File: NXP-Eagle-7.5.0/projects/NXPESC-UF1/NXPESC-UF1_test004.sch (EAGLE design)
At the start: 63 parts, among them J2 FLH1-03SZ-S3A-T, U1 MKV31F512VLL12-M, U10 PSMN1R4-30YLD, U11 PSMN1R4-30YLD, U12 PSMN1R4-30YLD, U13 PSMN1R4-30YLD, U2 MKV31F512VLH12-M, U8 PSMN1R4-30YLD, U9 PSMN1R4-30YLD

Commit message: connected additional signals to gate driver
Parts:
- removed U1: MKV31F512VLL12-M, MKV31F512VLL12:MKV31F512VLL12-M
- added D1, D2, D3: (no value), etc-diode_002a:DIODE-SOD323-R
- added R29, R30, R31: RESC0603-100R, etc_rcl:RESC0603-100R
- added U15: TJA1042TK/3, TJA1042T:TJA1042TK/3
- added U17: DF13-4P-1.25H, pixhawk2:DF13-4P-1.25H
- C1: value (none) -> Find a 50V
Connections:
- net N$7 renamed PWM_BT
- net N$8 renamed PWM_BB
- new net +5V: U15.VCC
- new net CAN0_RX: U15.RXD, U2.PTA13/LLWU_P4
- new net CAN0_TX: U15.TXD, U2.PTA12
- new net N$15: D3.C, U$1.VB1
- new net N$16: D2.C, U$1.VB2
- new net N$18: D1.C, U$1.VB3
- new net N$22: U15.CANH, U17-2.S
- new net N$23: U15.CANL, U17-3.S
- new net N$7: D3.A, R31.2
- new net N$8: R29.1, R30.1, R31.1
- new net PWM_AB: U$1.LIN1, U2.PTC2
- new net PWM_AT: U$1.HIN1, U2.PTC1/LLWU_P6
- new net PWM_CB: U$1.LIN3, U2.PTD5
- new net PWM_CT: U$1.HIN3, U2.PTD4/LLWU_P14
- new net STB: U15.STB, U2.PTA5
- net +3V3: now also U15.VIO, U2.VDD_2, U2.VDD_3; no longer U1.VDD, U1.VDD_2, U1.VDD_4, U1.VDD_5, U1.VDD_6, U2.PTE24, U2.VSS_3
- net GND: now also U15.GND, U17-4.S, U2.VSS_2, U2.VSS_3; no longer U1.VSS, U1.VSS_2, U1.VSS_4, U1.VSS_5, U1.VSS_6, U2.PTA18, U2.PTE25
- net N$5: now also D1.A, R29.2; no longer U$1.HIN1, U1.PTC1/LLWU_P6, U2.PTC1/LLWU_P6
- net N$6: now also D2.A, R30.2; no longer U$1.LIN1, U1.PTC2, U2.PTC2
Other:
- note added: "Need to define exact pinout"
- note added: "Verify against KV11 board This GPIO picked at random"
- note added: "change to 10 ohm, check power"
- moved on the sheet: C1, U2

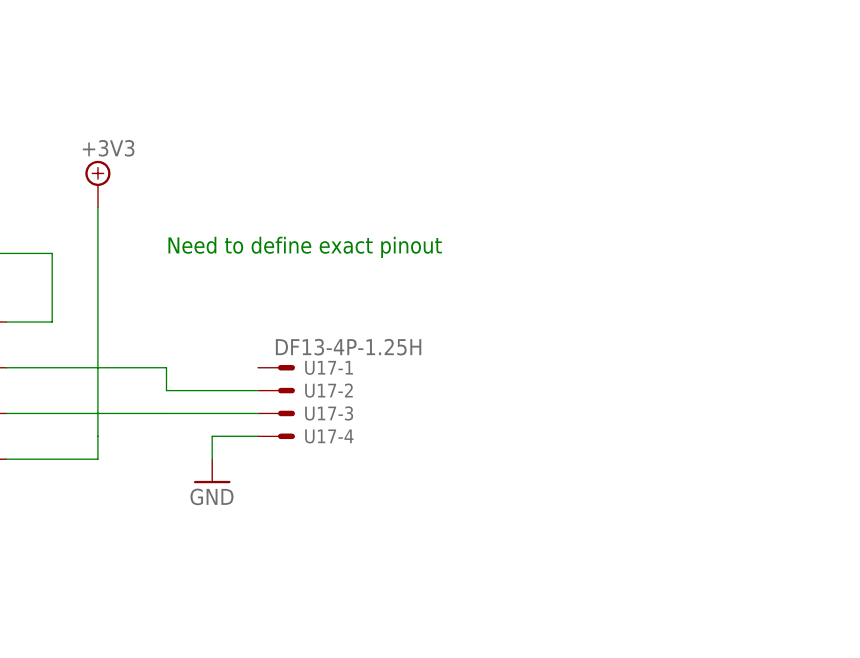
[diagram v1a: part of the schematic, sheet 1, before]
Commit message: moved from rev 003 to 004, merged in Gallowaa CAN conenctor additions.
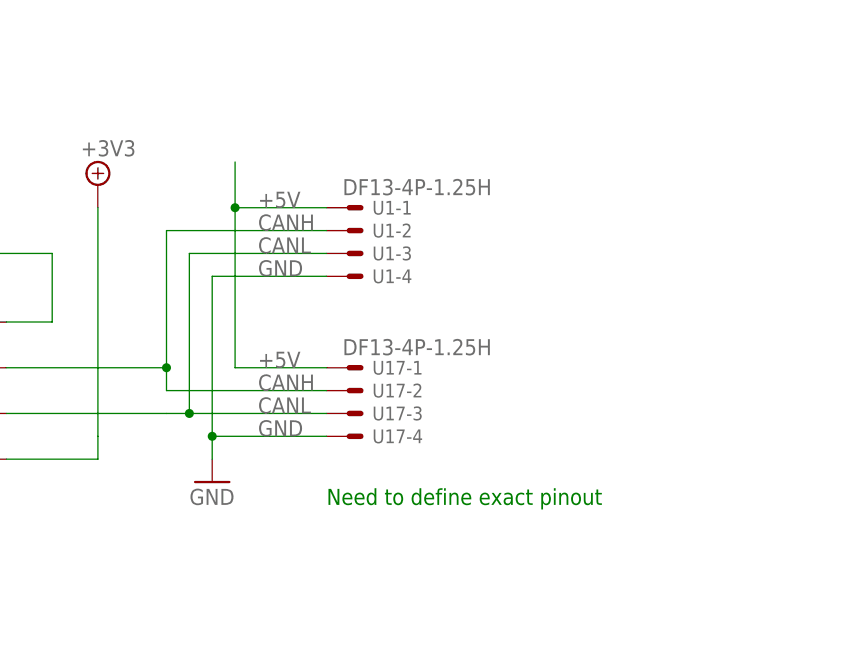
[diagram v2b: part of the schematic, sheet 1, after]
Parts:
- added U1: DF13-4P-1.25H, pixhawk2:DF13-4P-1.25H
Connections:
- removed net N$22: U15.CANH, U17-2.S
- removed net N$23: U15.CANL, U17-3.S
- new net CANH: U1-2.S, U15.CANH, U17-2.S
- new net CANL: U1-3.S, U15.CANL, U17-3.S
- net +5V: now also U1-1.S, U17-1.S
- net GND: now also U1-4.S
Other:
- moved on the sheet: U17-1, U17-2, U17-3, U17-4

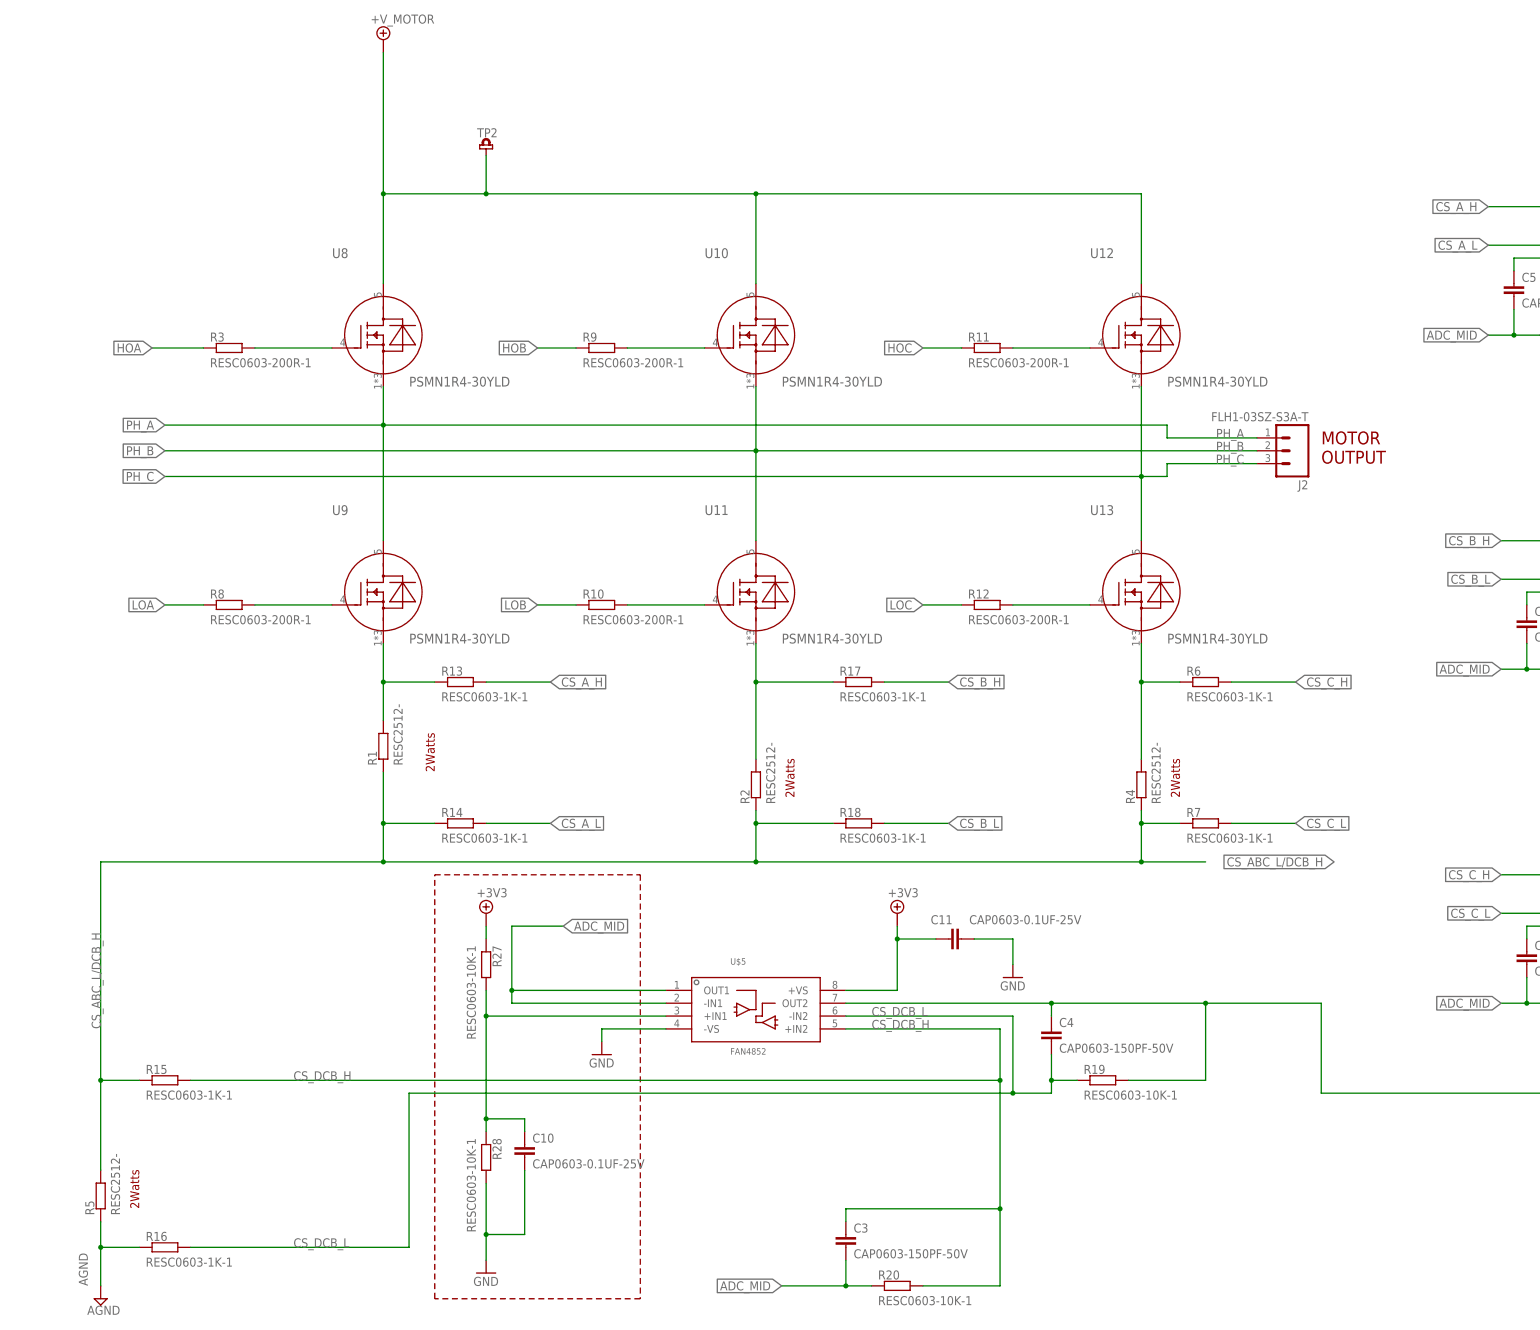
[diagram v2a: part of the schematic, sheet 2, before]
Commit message: more test routing. layout is tight but looks possible. Need to switch back to schematic to add missing parts (regulators, connectors, capacitors.)
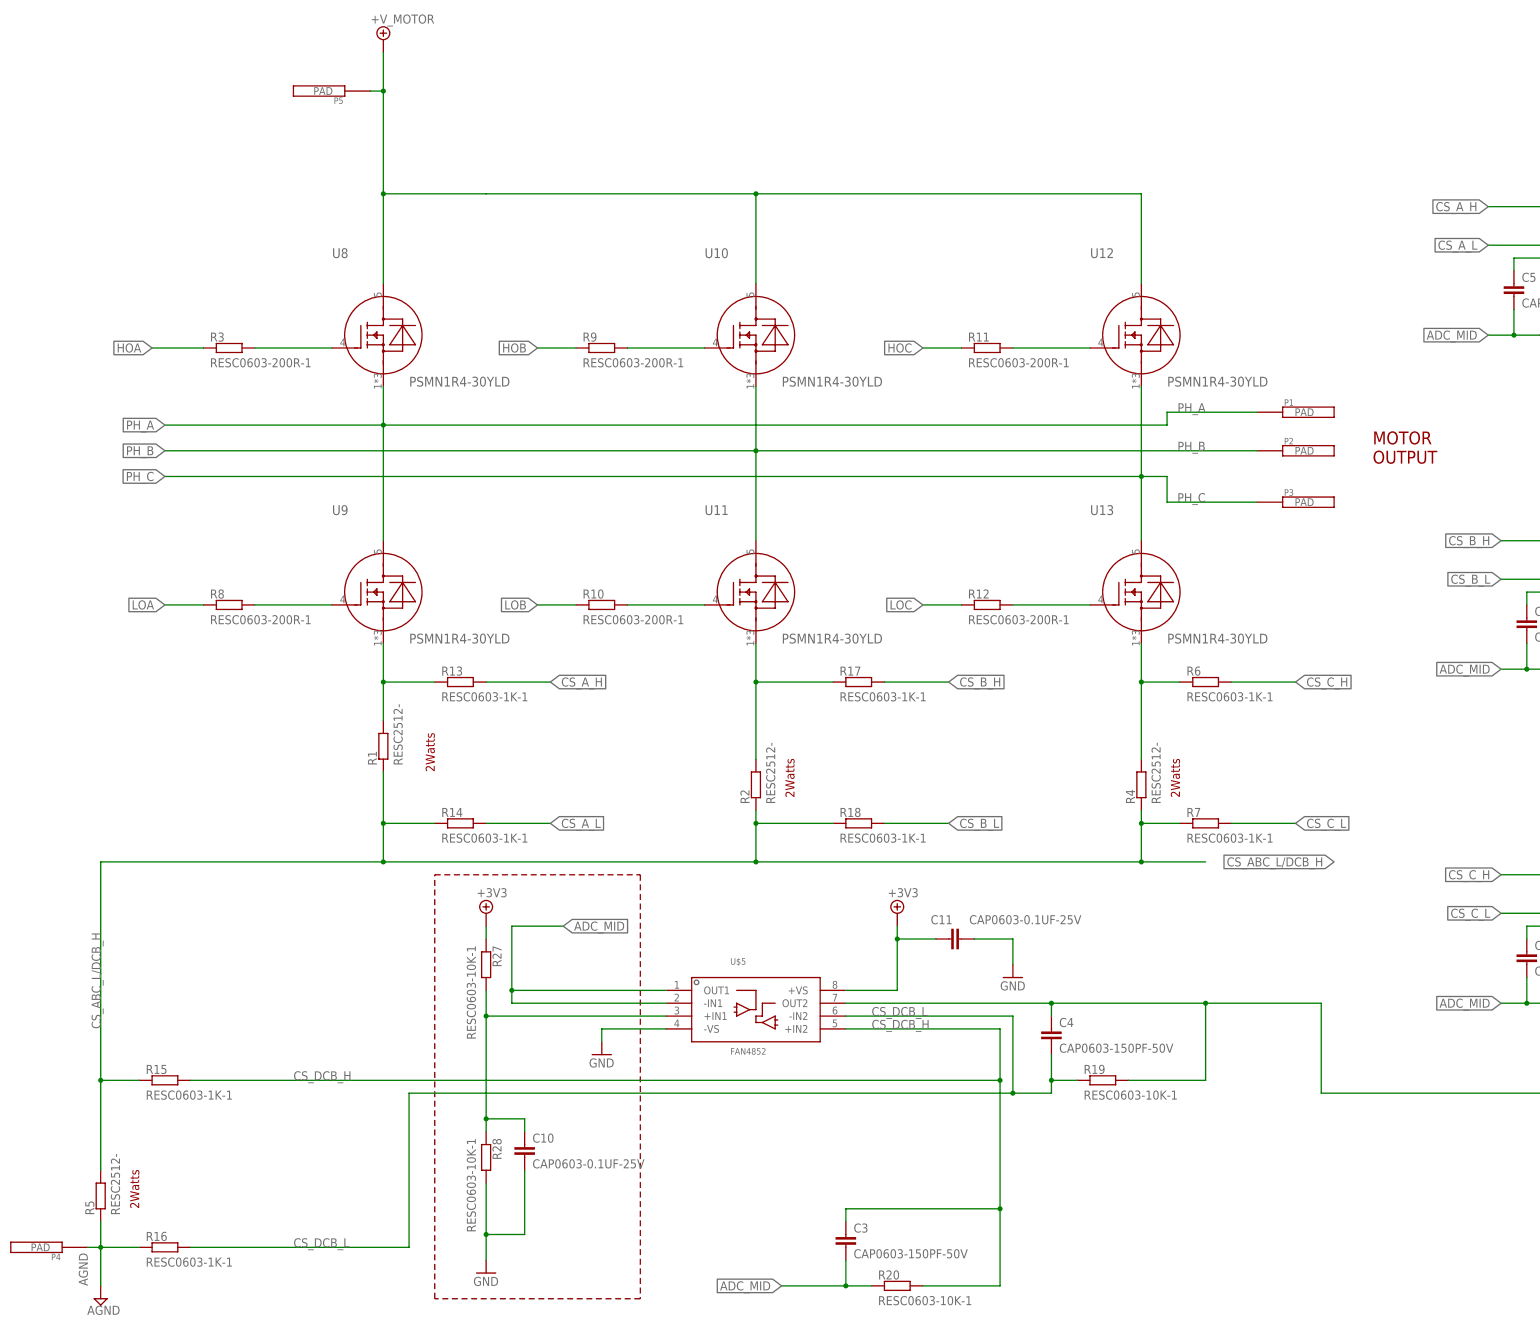
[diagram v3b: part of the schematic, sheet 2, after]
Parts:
- removed J2: FLH1-03SZ-S3A-T, etc-connector-003a:FLH1-03SZ-S3A-T
- removed TP2: +V_MOTOR, etc-connector-003a:TP-TH-SMLL
- added P1, P2, P3, P4, P5: MOT_PWR_PAD-1, NXPHLITE:MOT_PWR_PAD-1
- added U$15: CONN_CAN-SMD, pixhawk2:CONN_CAN-SMD
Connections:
- net +V_MOTOR: now also P5.PAD; no longer TP2.1
- net AGND: now also P4.PAD
- net PH_A: now also P1.PAD; no longer J2.1
- net PH_B: now also P2.PAD; no longer J2.2
- net PH_C: now also P3.PAD; no longer J2.3
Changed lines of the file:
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@@
 <part name="R11" library="etc-rcl" deviceset="RESC?-*" device="0603" technology="200R-1"/>
 <part name="R12" library="etc-rcl" deviceset="RESC?-*" device="0603" technology="200R-1"/>
-<part name="J2" library="etc-connector-003a" deviceset="FLH1-03SZ-S3A-T" device=""/>
-<part name="TP2" library="etc-connector-003a" deviceset="TP-TH-SMLL" device="" value="+V_MOTOR"/>
 <part name="FRAME2" library="NXPHLITE" deviceset="FRAME_B_L" device=""/>
 <part name="FRAME3" library="NXPHLITE" deviceset="FRAME_B_L" device=""/>
@@
 <part name="R31" library="etc_rcl" deviceset="RESC?-*" device="0603" technology="100R" value="RESC0603-100R"/>
 <part name="U1" library="pixhawk2" deviceset="DF13-4P-1.25?" device="H"/>
+<part name="U$15" library="pixhawk2" deviceset="CONN_CAN" device="-SMD"/>
+<part name="P1" library="NXPHLITE" deviceset="MOT_PWR_PAD" device="-1"/>
+<part name="P2" library="NXPHLITE" deviceset="MOT_PWR_PAD" device="-1"/>
+<part name="P3" library="NXPHLITE" deviceset="MOT_PWR_PAD" device="-1"/>
+<part name="P4" library="NXPHLITE" deviceset="MOT_PWR_PAD" device="-1"/>
+<part name="P5" library="NXPHLITE" deviceset="MOT_PWR_PAD" device="-1"/>
 </parts>
 <sheets>
@@
 <instance part="U1" gate="-3" x="213.36" y="45.72"/>
 <instance part="U1" gate="-4" x="213.36" y="43.18"/>
+<instance part="U$15" gate="-CAN_V+" x="210.82" y="68.58"/>
+<instance part="U$15" gate="-CAN_H" x="210.82" y="66.04"/>
+<instance part="U$15" gate="-CAN_L" x="210.82" y="63.5"/>
+<instance part="U$15" gate="-CAN_GND" x="210.82" y="60.96"/>
 </instances>
 <busses>
@@
 <sheet>
 <plain>
-<text x="266.7" y="172.72" size="2.54" layer="94">MOTOR
+<text x="276.86" y="172.72" size="2.54" layer="94">MOTOR
 OUTPUT</text>
 <circle x="81.28" y="116.84" radius="13.678315625" width="0.1524" layer="100"/>
@@
 <instance part="R11" gate="G$1" x="200.66" y="195.58"/>
 <instance part="R12" gate="G$1" x="200.66" y="144.78"/>
-<instance part="J2" gate="G$1" x="261.62" y="175.26" rot="R180"/>
-<instance part="TP2" gate="G$1" x="101.6" y="233.68"/>
 <instance part="FRAME2" gate="G$1" x="0" y="0"/>
 <instance part="FRAME2" gate="G$2" x="325.12" y="0"/>
@@
 <instance part="GND11" gate="1" x="124.46" y="55.88"/>
 <instance part="GND12" gate="1" x="205.74" y="71.12"/>
+<instance part="P1" gate="G$1" x="264.16" y="182.88"/>
+<instance part="P2" gate="G$1" x="264.16" y="175.26"/>
+<instance part="P3" gate="G$1" x="264.16" y="165.1"/>
+<instance part="P4" gate="G$1" x="12.7" y="17.78" rot="R180"/>
+<instance part="P5" gate="G$1" x="68.58" y="246.38" rot="R180"/>
 </instances>
 <busses>
@@
 <wire x1="81.28" y1="180.34" x2="236.22" y2="180.34" width="0.1524" layer="91"/>
 <label x="38.1" y="180.34" size="1.778" layer="95" rot="R180" xref="yes"/>
-<pinref part="J2" gate="G$1" pin="1"/>
-<wire x1="254" y1="177.8" x2="236.22" y2="177.8" width="0.1524" layer="91"/>
-<wire x1="236.22" y1="177.8" x2="236.22" y2="180.34" width="0.1524" layer="91"/>
-<label x="251.46" y="177.8" size="1.778" layer="95" rot="MR0"/>
+<wire x1="254" y1="182.88" x2="236.22" y2="182.88" width="0.1524" layer="91"/>
+<wire x1="236.22" y1="182.88" x2="236.22" y2="180.34" width="0.1524" layer="91"/>
+<label x="243.84" y="182.88" size="1.778" layer="95" rot="MR0"/>
+<pinref part="P1" gate="G$1" pin="PAD"/>
 </segment>
 </net>
@@
 <junction x="154.94" y="175.26"/>
 <label x="38.1" y="175.26" size="1.778" layer="95" rot="R180" xref="yes"/>
-<pinref part="J2" gate="G$1" pin="2"/>
-<label x="251.46" y="175.26" size="1.778" layer="95" rot="MR0"/>
+<label x="243.84" y="175.26" size="1.778" layer="95" rot="MR0"/>
+<pinref part="P2" gate="G$1" pin="PAD"/>
 </segment>
 </net>
@@
 <wire x1="231.14" y1="170.18" x2="236.22" y2="170.18" width="0.1524" layer="91"/>
 <label x="38.1" y="170.18" size="1.778" layer="95" rot="R180" xref="yes"/>
-<pinref part="J2" gate="G$1" pin="3"/>
-<wire x1="254" y1="172.72" x2="236.22" y2="172.72" width="0.1524" layer="91"/>
-<wire x1="236.22" y1="172.72" x2="236.22" y2="170.18" width="0.1524" layer="91"/>
-<label x="251.46" y="172.72" size="1.778" layer="95" rot="MR0"/>
+<wire x1="254" y1="165.1" x2="236.22" y2="165.1" width="0.1524" layer="91"/>
+<wire x1="236.22" y1="165.1" x2="236.22" y2="170.18" width="0.1524" layer="91"/>
+<label x="243.84" y="165.1" size="1.778" layer="95" rot="MR0"/>
+<pinref part="P3" gate="G$1" pin="PAD"/>
 </segment>
 </net>
@@
 <wire x1="154.94" y1="208.28" x2="154.94" y2="226.06" width="0.1524" layer="91"/>
 <junction x="154.94" y="226.06"/>
-<pinref part="TP2" gate="G$1" pin="1"/>
-<wire x1="101.6" y1="233.68" x2="101.6" y2="226.06" width="0.1524" layer="91"/>
-<junction x="101.6" y="226.06"/>
-<wire x1="81.28" y1="226.06" x2="81.28" y2="254" width="0.1524" layer="91"/>
+<wire x1="81.28" y1="226.06" x2="81.28" y2="246.38" width="0.1524" layer="91"/>
 <junction x="81.28" y="226.06"/>
 <pinref part="U$2" gate="G$1" pin="+V_MOTOR"/>
+<pinref part="P5" gate="G$1" pin="PAD"/>
+<wire x1="81.28" y1="246.38" x2="81.28" y2="254" width="0.1524" layer="91"/>
+<wire x1="78.74" y1="246.38" x2="81.28" y2="246.38" width="0.1524" layer="91"/>
+<junction x="81.28" y="246.38"/>
 </segment>
 </net>
@@
 <junction x="25.4" y="17.78"/>
 <label x="22.86" y="10.16" size="1.778" layer="95" rot="R90"/>
-</segment>
-</net>
+<pinref part="P4" gate="G$1" pin="PAD"/>
+<wire x1="22.86" y1="17.78" x2="25.4" y2="17.78" width="0.1524" layer="91"/>
+</segment>
+</net>

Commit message: Majority of Power FET stage/gate driver and sense amplifiers are layed out. Moving on to finishing the MCU details.
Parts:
- removed H3: TC2050-IDCNH, etc-connector-003a:TC2050-IDCNH
- added C19: (no value), etc-rcl:CPOL-USETR1
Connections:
- net +3V3: no longer H3.VCC
- net +V_MOTOR: now also C19.+
- net AGND: now also C19.-
- net GND: no longer H3.GND, H3.TMS
- net RESET_B: no longer H3.TDO
- net SWD_CLK: no longer H3.NOTUSED@2
- net SWD_DIO: no longer H3.RESET
- net TRACE_SWO: no longer H3.TDI
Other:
- note added: "This CAP for footprint only. Will need to be modified. Elecrtolytic CAP hangs off side of board."

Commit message: Reviewing NXPESC-UF1/NXPESC-UF1_test004.sch schematic, comparing against SCHEMATICS-FRDM-mc-lvpmsm-sch.pdf
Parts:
- added C20, C21, C22: CAP0603-1UF-50V, etc-rcl:CAP0603-1UF-50V
- added CA1: CCA-GNM-314R71C104MA01L, etc-rcl:CCA-GNM-314R71C104MA01L
- added J1: ARM_MINI_JTAG-TH, pixhawk2:ARM_MINI_JTAG-TH
- added P15: DF13-6P-1.25H, pixhawk2:DF13-6P-1.25H
- added P18: DF13-5P-1.25H, pixhawk2:DF13-5P-1.25H
- added P8: DF13-4P-1.25H, pixhawk2:DF13-4P-1.25H
- added R42: (no value), pixhawk2:RESISTOR0402-RES
- added RN1, RN2, RN3: CTS742C083, pixhawk2:CTS742C083
- added SH1: RESC0603-0R, etc-rcl:RESC0603-0R
- C1: value Find a 50V -> CAP0603-1UF-50V; device pixhawk2:CAP_POL1206 -> etc-rcl:CAP0603-1UF-50V
- R29, R30, R31: value RESC0603-100R -> RESC0603-10R-1; device etc_rcl:RESC0603-100R -> etc-rcl:RESC0603-10R-1
- U1: value DF13-4P-1.25H -> 74LVX14MTCX; device pixhawk2:DF13-4P-1.25H -> 74LVX14MTCX:74LVX14MTCX
- renumbered U17 to P9
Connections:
- removed net N$8: R29.1, R30.1, R31.1
- new net ENC_A: U1.~O3, U2.PTB18
- new net ENC_B: U1.~O4, U2.PTB19
- new net ENC_C: U1.~O5
- new net N$19: U1.I5, U1.~O0
- new net N$20: CA1.RA1, RN2.8, RN3.4
- new net N$21: CA1.RB1, RN2.7, RN3.3
- new net N$22: CA1.RC1, RN2.6, RN3.2
- new net N$23: U1.I4, U1.~O1
- new net N$24: U1.I3, U1.~O2
- new net N$25: RN3.7, U1.I0
- new net N$26: RN3.6, U1.I1
- new net N$27: RN3.5, U1.I2
- new net N$29: P18-3.S, RN1.3, RN2.3
- new net N$32: P18-4.S, RN1.2, RN2.2
- new net N$35: P18-5.S, RN1.1, RN2.1
- net +3V3: no longer C1.+, U$1.VDD
- net +5V: now also P18-1.S, P8-1.S, RN1.6, RN1.7, RN1.8, U1.VCC; no longer U1-1.S
- net +V_MOTOR: now also C21.1, R29.1, R30.1, R31.1, U$1.VDD
- net AGND: now also SH1.1
- net CANH: now also P8-2.S; no longer U1-2.S
- net CANL: now also P8-3.S; no longer U1-3.S
- net GND: now also C21.2, CA1.RA2, CA1.RB2, CA1.RC2, P18-2.S, P8-4.S, SH1.2, U1.GND; no longer C1.-, U1-4.S
- net N$15: now also C1.1
- net N$16: now also C20.1
- net N$18: now also C22.1
- net PH_A: now also C1.2
- net PH_B: now also C20.2
- net PH_C: now also C22.2
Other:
- note added: "(TJA1051 instead?)"
- note added: "ADC Midpoint Ref"
- note added: "Encoder C needs a home. Currently taken by CANRX!"
- note added: "Extra op-amp Not used"
- note added: "NOTE: Changed from FRDM LVPMSM design No 15V regulation on this supply! expecting 3S (11V) input"
- note added: "This CAP for footprint only. Will need to be modified. Electrolytic CAP hangs off side of board. 3x 220uF 100V was on KV board 390uf@100V 18x22mm with 0.295"(7.5mm) lead spacing is available."
- note removed: "This CAP for footprint only. Will need to be modified. Elecrtolytic CAP hangs off side of board."
- note removed: "change to 10 ohm, check power"
